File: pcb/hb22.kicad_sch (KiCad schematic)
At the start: 11 parts

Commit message: Use normal SMD footprints, avoid handsolder.
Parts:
- R6, R7: footprint Resistor_SMD:R_0805_2012Metric_Pad1.20x1.40mm_HandSolder -> Resistor_SMD:R_0805_2012Metric
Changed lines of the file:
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@@
 			)
 		)
-		(property "Footprint" "Resistor_SMD:R_0805_2012Metric_Pad1.20x1.40mm_HandSolder"
+		(property "Footprint" "Resistor_SMD:R_0805_2012Metric"
 			(at 66.802 77.47 90)
 			(effects
@@
 			)
 		)
-		(property "Footprint" "Resistor_SMD:R_0805_2012Metric_Pad1.20x1.40mm_HandSolder"
+		(property "Footprint" "Resistor_SMD:R_0805_2012Metric"
 			(at 61.722 77.47 90)
 			(effects

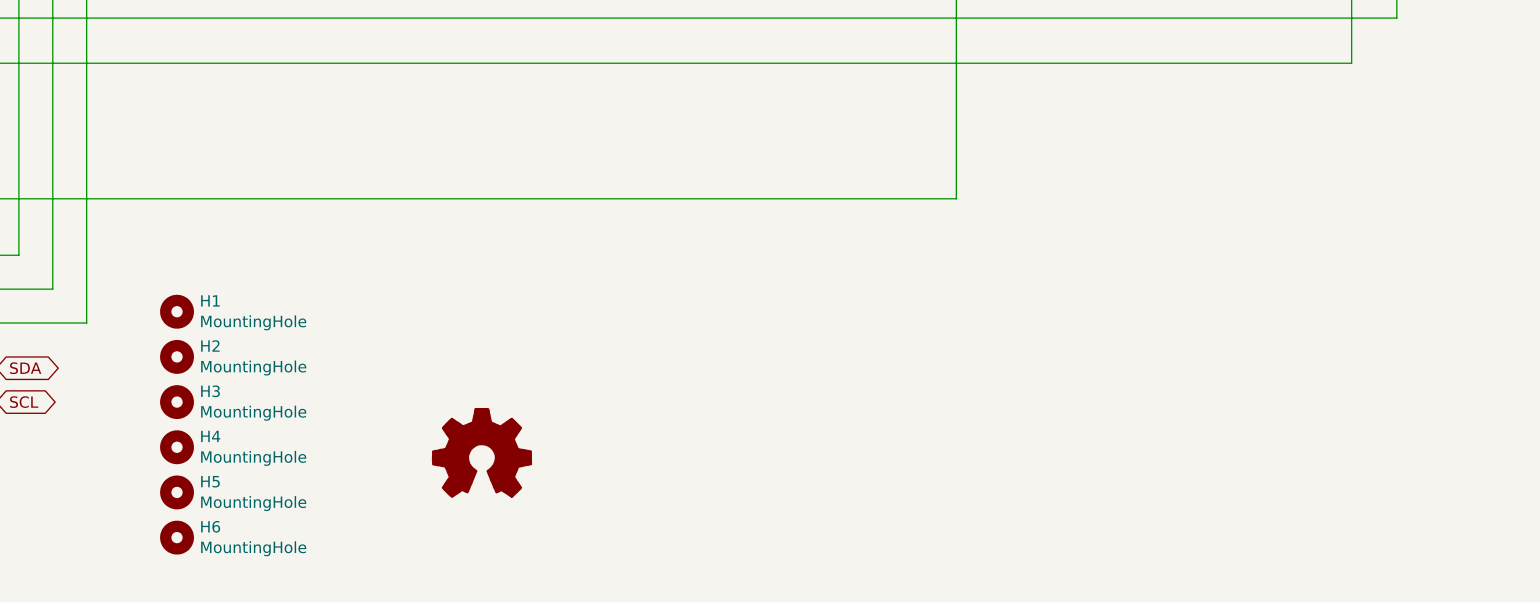
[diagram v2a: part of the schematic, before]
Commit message: Add stabil heatsinks, minor improvements.
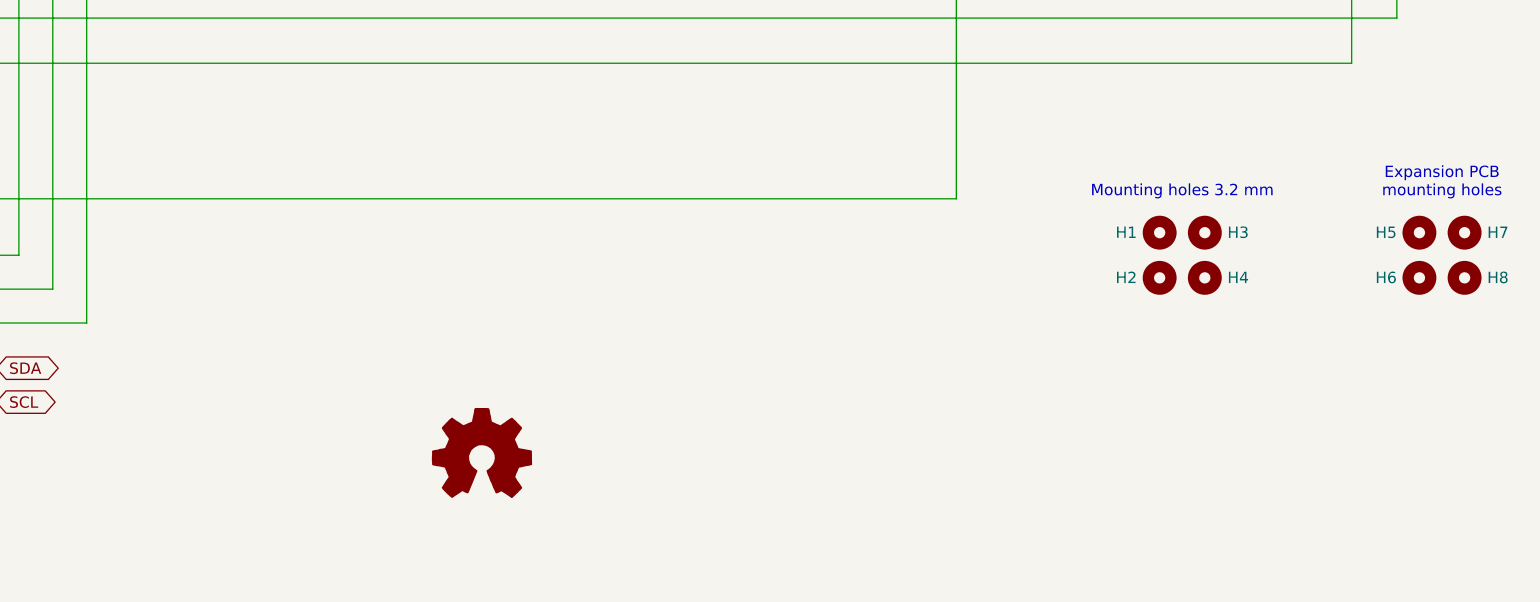
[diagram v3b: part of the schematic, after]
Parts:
- added H7, H8: ~, MountingHole:MountingHole_3.2mm_M3_Pad, symbol Mechanical:MountingHole
- H1, H2, H3, H4, H5, H6: value MountingHole -> ~; footprint MountingHole:MountingHole_3.2mm_M3_Pad_Via -> MountingHole:MountingHole_3.2mm_M3_Pad
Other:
- note added: "Expansion PCB mounting holes"
- note added: "Mounting holes 3.2 mm"
- moved on the sheet: H1, H2, H3, H4, H5, H6

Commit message: exp-mtb: use standard SMD packages, no handsolder.
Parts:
- TP1: footprint TestPoint:TestPoint_Loop_D3.50mm_Drill1.4mm_Beaded -> TestPoint:TestPoint_Loop_D1.80mm_Drill1.0mm_Beaded
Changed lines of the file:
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@@
 			)
 		)
-		(property "Footprint" "TestPoint:TestPoint_Loop_D3.50mm_Drill1.4mm_Beaded"
+		(property "Footprint" "TestPoint:TestPoint_Loop_D1.80mm_Drill1.0mm_Beaded"
 			(at 106.68 82.55 0)
 			(effects
